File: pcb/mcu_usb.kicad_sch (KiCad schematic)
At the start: 33 parts, among them J12 USB_C_Receptacle, J13 UPDI, U10 CP2102N-A02-GQFN24, U11 LP2985-3.3, U9 AVR128DA32-I/PT, Y1 32.768kHz

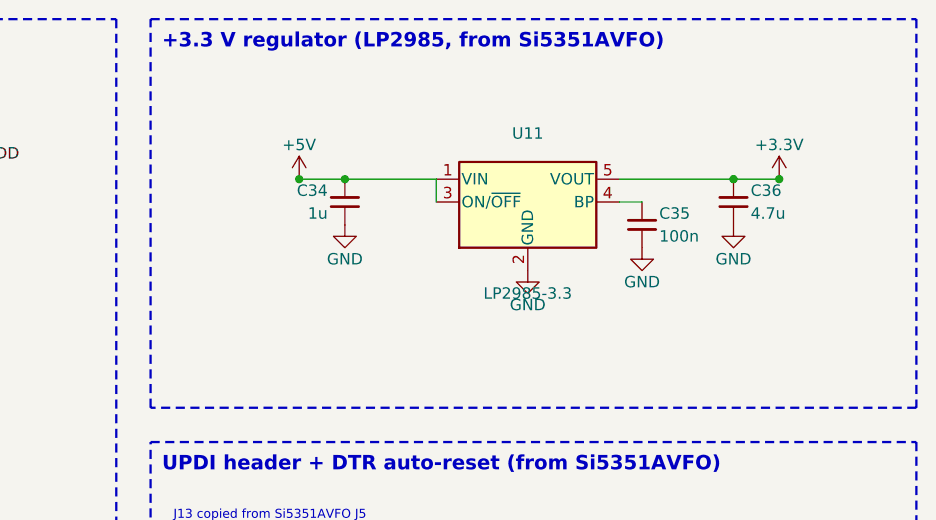
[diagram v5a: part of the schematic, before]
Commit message: GPS fixes: TPS22941 antenna current limit, TLV75533 500 mA LDO, CR1220 V_BCKP
- U13 TPS22941 (C2653762) limits antenna short to 40-80 mA with auto-restart
  (avg <= 27 mA, was 320 mA); OC -> SDA as ANT_SHORT_N (IM 3.3.1.2)
- U11 LP2985 -> TLV75533PDBVR (C404027), C35 removed (pin 4 NC)
- C47/D13/R41 removed; BT1 CR1220 in KH-BS1220-2-SMT (C5365932)
- VERIFY updated
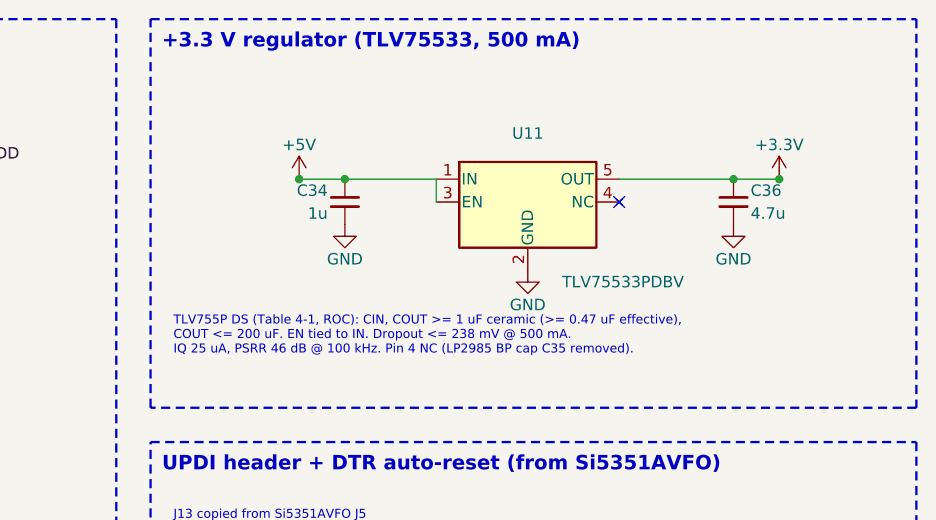
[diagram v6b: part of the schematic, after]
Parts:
- removed C35: 100n, Capacitor_SMD:C_0805_2012Metric, symbol Device:C_Small
- removed U11: LP2985-3.3, Package_TO_SOT_SMD:SOT-23-5, symbol Regulator_Linear:LP2985-3.3
- added U11: TLV75533PDBV, Package_TO_SOT_SMD:SOT-23-5, symbol OpenBeacon2:TLV75533PDBV
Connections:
- net +3.3V: now also U11.5 (OUT)
- net +5V: now also U11.1 (IN), U11.3 (EN)
- net GND: now also U11.2 (GND)
- no-connect marks 15 -> 16
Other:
- note added: "+3.3 V regulator (TLV75533, 500 mA)"
- note added: "TLV755P DS (Table 4-1, ROC): CIN, COUT >= 1 uF ceramic (>= 0.47 uF effective), COUT <= 200 uF. EN tied to IN. Dropout <= 238 mV @ 500 mA. IQ 25 uA, PSRR 46 dB @ 100 kHz. Pin 4 NC (LP2985 BP cap C35 removed)."
- note removed: "+3.3 V regulator (LP2985, from Si5351AVFO)"
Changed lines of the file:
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@@
 		)
 	)
-	(text "+3.3 V regulator (LP2985, from Si5351AVFO)"
+	(text "+3.3 V regulator (TLV75533, 500 mA)"
 		(exclude_from_sim no)
 		(at 200.66 22.86 0)
@@
 	)
 	(symbol
-		(lib_id "Regulator_Linear:LP2985-3.3")
+		(lib_id "OpenBeacon2:TLV75533PDBV")
 		(at 241.3 40.64 0)
 		(unit 1)
@@
 			)
 		)
-		(property "Value" "LP2985-3.3"
-			(at 241.3 50.8 0)
+		(property "Value" "TLV75533PDBV"
+			(at 245.11 49.53 0)
 			(effects
 				(font
 					(size 1.27 1.27)
 				)
+				(justify left)
 			)
 		)
@@
 			)
 		)
-		(property "Datasheet" ""
+		(property "Datasheet" "https://www.ti.com/lit/ds/symlink/tlv755p.pdf"
 			(at 241.3 40.64 0)
 			(effects
@@
 			)
 		)
-		(property "MPN" "LP2985AIM5-3.3/NOPB"
+		(property "MPN" "TLV75533PDBVR"
 			(at 241.3 40.64 0)
 			(effects
@@
 			)
 		)
-		(property "LCSC" "C16085"
+		(property "LCSC" "C404027"
 			(at 241.3 40.64 0)
 			(effects
@@
 		(pin "1"
 		)
-		(pin "2"
-		)
 		(pin "3"
 		)
+		(pin "2"
+		)
 		(pin "4"
 		)
@@
 		)
 	)
-	(wire
-		(pts
-			(xy 251.46 40.64)
-			(xy 254 40.64)
-		)
-		(stroke
-			(width 0)
-			(type default)
-		)
-	)
-	(symbol
-		(lib_id "Device:C_Small")
-		(at 254 43.18 0)
-		(unit 1)
-		(exclude_from_sim no)
-		(in_bom yes)
-		(on_board yes)
-		(dnp no)
-		(property "Reference" "C35"
-			(at 255.905 41.91 0)
-			(effects
-				(font
-					(size 1.27 1.27)
-				)
-				(justify left)
-			)
-		)
-		(property "Value" "100n"
-			(at 255.905 44.45 0)
-			(effects
-				(font
-					(size 1.27 1.27)
-				)
-				(justify left)
-			)
-		)
-		(property "Footprint" "Capacitor_SMD:C_0805_2012Metric"
-			(at 254 43.18 0)
-			(effects
-				(font
-					(size 1.27 1.27)
-				)
-				(hide yes)
-			)
-		)
-		(property "Datasheet" ""
-			(at 254 43.18 0)
-			(effects
-				(font
-					(size 1.27 1.27)
-				)
-				(hide yes)
-			)
-		)
-		(property "MPN" "CC0805KRX7R9BB104"
-			(at 254 43.18 0)
-			(effects
-				(font
-					(size 1.27 1.27)
-				)
-				(hide yes)
-			)
-		)
-		(property "Manufacturer" "YAGEO"
-			(at 254 43.18 0)
-			(effects
-				(font
-					(size 1.27 1.27)
-				)
-				(hide yes)
-			)
-		)
-		(property "LCSC" "C49678"
-			(at 254 43.18 0)
-			(effects
-				(font
-					(size 1.27 1.27)
-				)
-				(hide yes)
-			)
-		)
-		(pin "1"
-		)
-		(pin "2"
-		)
-		(instances
-			(project "OpenBeacon2"
-				(path "/046319a3-a6ce-4e59-a888-94e340127381/5d0c3a21-8e4b-4c7a-9a61-0b2f6e7a9c11"
-					(reference "C35")
-					(unit 1)
-				)
-			)
-		)
-	)
-	(symbol
-		(lib_id "power:GND")
-		(at 254 45.72 0)
-		(unit 1)
-		(exclude_from_sim no)
-		(in_bom no)
-		(on_board yes)
-		(dnp no)
-		(property "Reference" "#PWR923"
-			(at 254 45.72 0)
-			(effects
-				(font
-					(size 1.27 1.27)
-				)
-				(hide yes)
-			)
-		)
-		(property "Value" "GND"
-			(at 254 49.53 0)
-			(effects
-				(font
-					(size 1.27 1.27)
-				)
-			)
-		)
-		(property "Footprint" ""
-			(at 254 45.72 0)
-			(effects
-				(font
-					(size 1.27 1.27)
-				)
-				(hide yes)
-			)
-		)
-		(property "Datasheet" ""
-			(at 254 45.72 0)
-			(effects
-				(font
-					(size 1.27 1.27)
-				)
-				(hide yes)
-			)
-		)
-		(pin "1"
-		)
-		(instances
-			(project "OpenBeacon2"
-				(path "/046319a3-a6ce-4e59-a888-94e340127381/5d0c3a21-8e4b-4c7a-9a61-0b2f6e7a9c11"
-					(reference "#PWR923")
-					(unit 1)
-				)
-			)
-		)
+	(no_connect
+		(at 251.46 40.64)
 	)
 	(wire
@@
 		(on_board yes)
 		(dnp no)
-		(property "Reference" "#PWR924"
+		(property "Reference" "#PWR923"
 			(at 264.16 43.18 0)
 			(effects
@@
 			(project "OpenBeacon2"
 				(path "/046319a3-a6ce-4e59-a888-94e340127381/5d0c3a21-8e4b-4c7a-9a61-0b2f6e7a9c11"
-					(reference "#PWR924")
+					(reference "#PWR923")
 					(unit 1)
 				)
@@
 		(on_board yes)
 		(dnp no)
-		(property "Reference" "#PWR925"
+		(property "Reference" "#PWR924"
 			(at 269.24 38.1 0)
 			(effects
@@
 			(project "OpenBeacon2"
 				(path "/046319a3-a6ce-4e59-a888-94e340127381/5d0c3a21-8e4b-4c7a-9a61-0b2f6e7a9c11"
-					(reference "#PWR925")
+					(reference "#PWR924")
 					(unit 1)
 				)
@@
 		(color 0 0 0 0)
 	)
+	(text "TLV755P DS (Table 4-1, ROC): CIN, COUT >= 1 uF ceramic (>= 0.47 uF effective),\nCOUT <= 200 uF. EN tied to IN. Dropout <= 238 mV @ 500 mA.\nIQ 25 uA, PSRR 46 dB @ 100 kHz. Pin 4 NC (LP2985 BP cap C35 removed)."
+		(exclude_from_sim no)
+		(at 201.93 53.34 0)
+		(effects
+			(font
+				(size 1.0 1.0)
+			)
+			(justify left top)
+		)
+	)
 	(rectangle
 		(start 199.39 67.31)
@@
 		(on_board yes)
 		(dnp no)
-		(property "Reference" "#PWR926"
+		(property "Reference" "#PWR925"
 			(at 269.24 81.28 0)
 			(effects
@@
 			(project "OpenBeacon2"
 				(path "/046319a3-a6ce-4e59-a888-94e340127381/5d0c3a21-8e4b-4c7a-9a61-0b2f6e7a9c11"
-					(reference "#PWR926")
+					(reference "#PWR925")
 					(unit 1)
 				)
@@
 		(on_board yes)
 		(dnp no)
-		(property "Reference" "#PWR927"
+		(property "Reference" "#PWR926"
 			(at 269.24 88.9 0)
 			(effects
@@
 			(project "OpenBeacon2"
 				(path "/046319a3-a6ce-4e59-a888-94e340127381/5d0c3a21-8e4b-4c7a-9a61-0b2f6e7a9c11"
-					(reference "#PWR927")
+					(reference "#PWR926")
 					(unit 1)
 				)
@@
 		(on_board yes)
 		(dnp no)
-		(property "Reference" "#PWR928"
+		(property "Reference" "#PWR927"
 			(at 224.79 109.22 0)
 			(effects
@@
 			(project "OpenBeacon2"
 				(path "/046319a3-a6ce-4e59-a888-94e340127381/5d0c3a21-8e4b-4c7a-9a61-0b2f6e7a9c11"
-					(reference "#PWR928")
+					(reference "#PWR927")
 					(unit 1)
 				)
@@
 		(on_board yes)
 		(dnp no)
-		(property "Reference" "#PWR929"
+		(property "Reference" "#PWR928"
 			(at 91.44 116.84 0)
 			(effects
@@
 			(project "OpenBeacon2"
 				(path "/046319a3-a6ce-4e59-a888-94e340127381/5d0c3a21-8e4b-4c7a-9a61-0b2f6e7a9c11"
-					(reference "#PWR929")
+					(reference "#PWR928")
 					(unit 1)
 				)
@@
 		(on_board yes)
 		(dnp no)
-		(property "Reference" "#PWR930"
+		(property "Reference" "#PWR929"
 			(at 81.28 116.84 0)
 			(effects
@@
 			(project "OpenBeacon2"
 				(path "/046319a3-a6ce-4e59-a888-94e340127381/5d0c3a21-8e4b-4c7a-9a61-0b2f6e7a9c11"
-					(reference "#PWR930")
+					(reference "#PWR929")
 					(unit 1)
 				)
@@
 		(on_board yes)
 		(dnp no)
-		(property "Reference" "#PWR931"
+		(property "Reference" "#PWR930"
 			(at 99.06 111.76 0)
 			(effects
@@
 			(project "OpenBeacon2"
 				(path "/046319a3-a6ce-4e59-a888-94e340127381/5d0c3a21-8e4b-4c7a-9a61-0b2f6e7a9c11"
-					(reference "#PWR931")
+					(reference "#PWR930")
 					(unit 1)
 				)
@@
 		(on_board yes)
 		(dnp no)
-		(property "Reference" "#PWR932"
+		(property "Reference" "#PWR931"
 			(at 114.3 116.84 0)
 			(effects
@@
 			(project "OpenBeacon2"
 				(path "/046319a3-a6ce-4e59-a888-94e340127381/5d0c3a21-8e4b-4c7a-9a61-0b2f6e7a9c11"
-					(reference "#PWR932")
+					(reference "#PWR931")
 					(unit 1)
 				)
@@
 		(on_board yes)
 		(dnp no)
-		(property "Reference" "#PWR933"
+		(property "Reference" "#PWR932"
 			(at 106.68 111.76 0)
 			(effects
@@
 			(project "OpenBeacon2"
 				(path "/046319a3-a6ce-4e59-a888-94e340127381/5d0c3a21-8e4b-4c7a-9a61-0b2f6e7a9c11"
-					(reference "#PWR933")
+					(reference "#PWR932")
 					(unit 1)
 				)
@@
 		(on_board yes)
 		(dnp no)
-		(property "Reference" "#PWR934"
+		(property "Reference" "#PWR933"
 			(at 101.6 175.26 0)
 			(effects
@@
 			(project "OpenBeacon2"
 				(path "/046319a3-a6ce-4e59-a888-94e340127381/5d0c3a21-8e4b-4c7a-9a61-0b2f6e7a9c11"
-					(reference "#PWR934")
+					(reference "#PWR933")
 					(unit 1)
 				)
@@
 		(on_board yes)
 		(dnp no)
-		(property "Reference" "#PWR935"
+		(property "Reference" "#PWR934"
 			(at 58.42 144.78 0)
 			(effects
@@
 			(project "OpenBeacon2"
 				(path "/046319a3-a6ce-4e59-a888-94e340127381/5d0c3a21-8e4b-4c7a-9a61-0b2f6e7a9c11"
-					(reference "#PWR935")
+					(reference "#PWR934")
 					(unit 1)
 				)
@@
 		(on_board yes)
 		(dnp no)
-		(property "Reference" "#PWR936"
+		(property "Reference" "#PWR935"
 			(at 129.54 182.88 0)
 			(effects
@@
 			(project "OpenBeacon2"
 				(path "/046319a3-a6ce-4e59-a888-94e340127381/5d0c3a21-8e4b-4c7a-9a61-0b2f6e7a9c11"
-					(reference "#PWR936")
+					(reference "#PWR935")
 					(unit 1)
 				)
@@
 		(on_board yes)
 		(dnp no)
-		(property "Reference" "#PWR937"
+		(property "Reference" "#PWR936"
 			(at 139.7 180.34 0)
 			(effects
@@
 			(project "OpenBeacon2"
 				(path "/046319a3-a6ce-4e59-a888-94e340127381/5d0c3a21-8e4b-4c7a-9a61-0b2f6e7a9c11"
-					(reference "#PWR937")
+					(reference "#PWR936")
 					(unit 1)
 				)

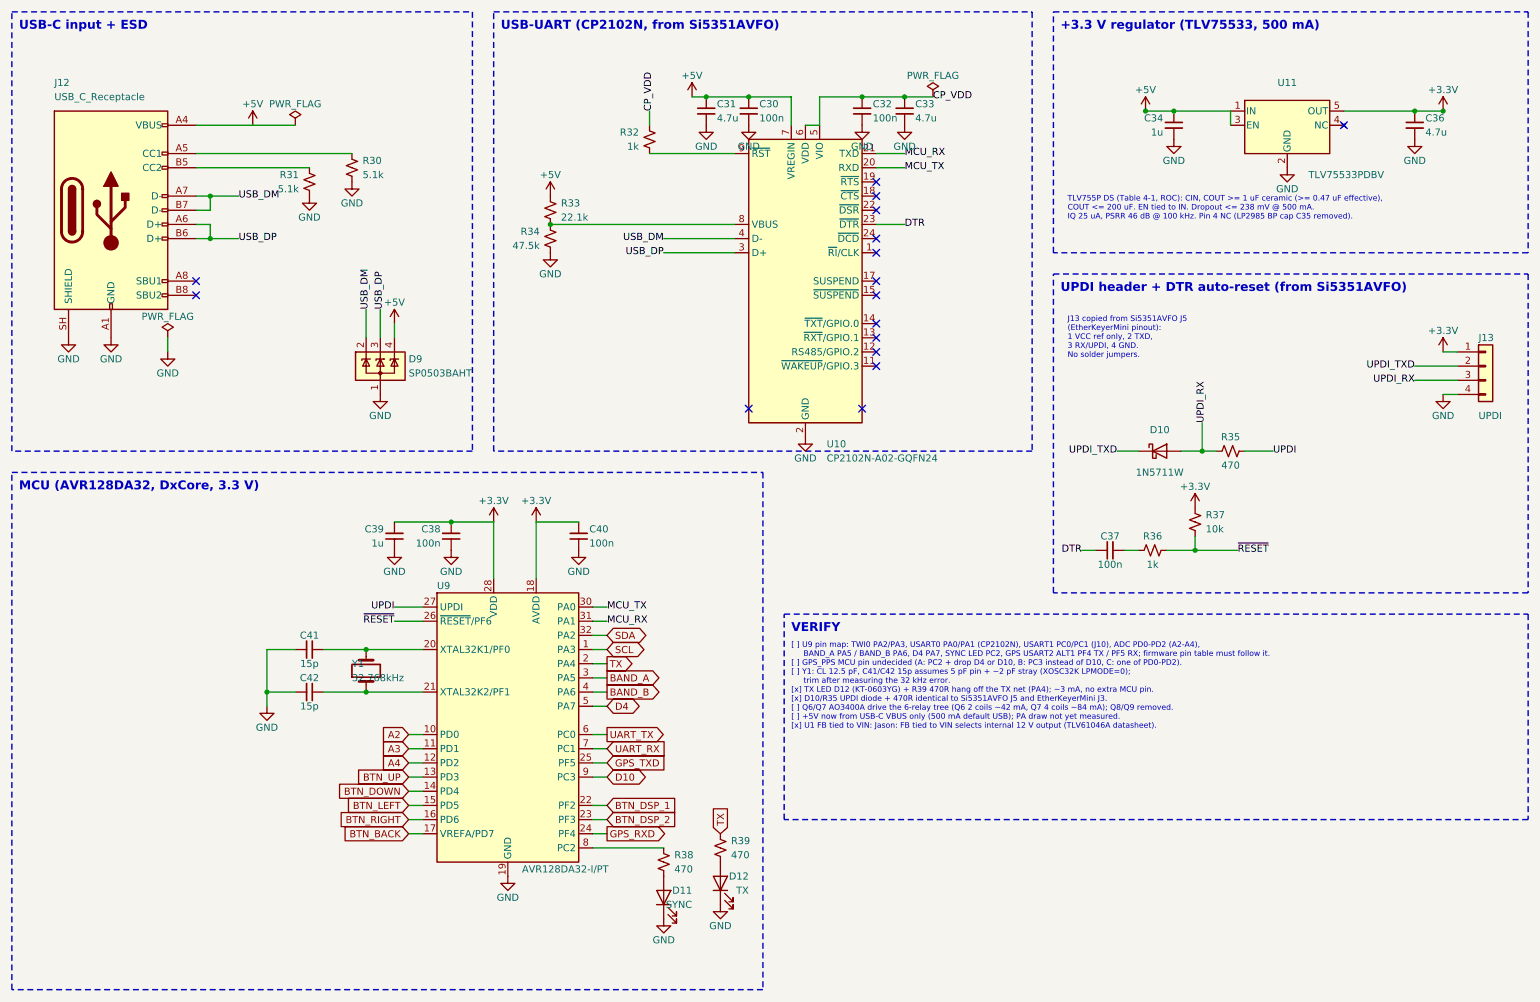
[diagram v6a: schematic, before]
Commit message: MCU: migrate to AVR128DA48-E/PT TQFP-48; GPS on USART3 PB0/PB1, GPS_PPS on async PF2 (EVSYS to TCB0 capture), per-pin decoupling
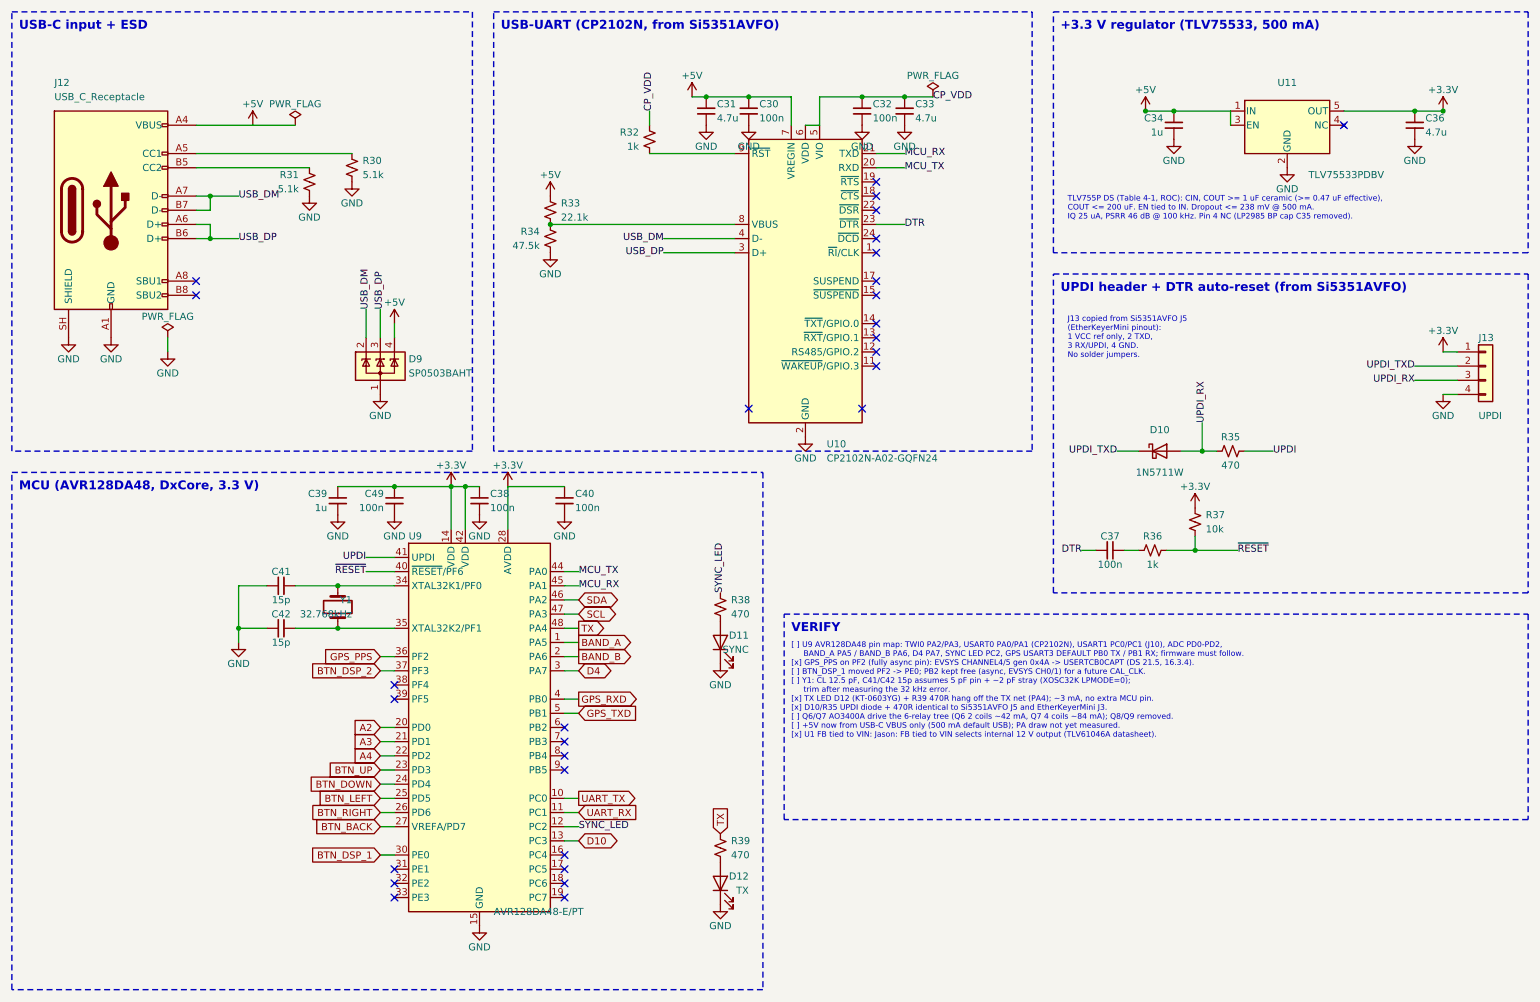
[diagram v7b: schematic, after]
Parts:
- removed U9: AVR128DA32-I/PT, Package_QFP:TQFP-32_7x7mm_P0.8mm, symbol OpenBeacon2:AVR128DA32x-xPT
- added C49: 100n, Capacitor_SMD:C_0603_1608Metric, symbol Device:C_Small
- added U9: AVR128DA48-E/PT, Package_QFP:TQFP-48_7x7mm_P0.5mm, symbol OpenBeacon2:AVR128DA48x-xPT
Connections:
- net +3.3V: now also C49.1, U9.14 (VDD), U9.28 (AVDD), U9.42 (VDD)
- net A2: now also U9.20 (PD0)
- net A3: now also U9.21 (PD1)
- net A4: now also U9.22 (PD2)
- net BAND_A: now also U9.1 (PA5)
- net BAND_B: now also U9.2 (PA6)
- net BTN_BACK: now also U9.27 (VREFA/PD7)
- net BTN_DOWN: now also U9.24 (PD4)
- net BTN_DSP_1: now also U9.30 (PE0)
- net BTN_DSP_2: now also U9.37 (PF3)
- net BTN_LEFT: now also U9.25 (PD5)
- net BTN_RIGHT: now also U9.26 (PD6)
- net BTN_UP: now also U9.23 (PD3)
- net D10: now also U9.13 (PC3)
- net D4: now also U9.3 (PA7)
- net GND: now also C49.2, U9.15 (GND), U9.29 (GND), U9.43 (GND)
- net GPS_RXD: now also U9.4 (PB0)
- net GPS_TXD: now also U9.5 (PB1)
- net MCU_RX: now also U9.45 (PA1)
- net MCU_TX: now also U9.44 (PA0)
- net SCL: now also U9.47 (PA3)
- net SDA: now also U9.46 (PA2)
- net TX: now also U9.48 (PA4)
- net UART_RX: now also U9.11 (PC1)
- net UART_TX: now also U9.10 (PC0)
- net UPDI: now also U9.41 (UPDI)
- net ~{RESET}: now also U9.40 (~{RESET}/PF6)
- net at C41.2, Y1.2: now also U9.34 (XTAL32K1/PF0)
- net SYNC_LED: now reaches R38.1
- net SYNC_LED: now also U9.12 (PC2)
- net at C42.2, Y1.1: now also U9.35 (XTAL32K2/PF1)
- new net GPS_PPS: U9.36 (PF2)
- no-connect marks 16 -> 29
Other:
- note added: "MCU (AVR128DA48, DxCore, 3.3 V)"
- note added: "[ ] U9 AVR128DA48 pin map: TWI0 PA2/PA3, USART0 PA0/PA1 (CP2102N), USART1 PC0/PC1 (J10), ADC PD0-PD2, BAND_A PA5 / BAND_B PA6, D4 PA7, SYNC LED PC2, GPS USART3 DEFAULT PB0 TX / PB1 RX; firmware must follow. [x] GPS_PPS on PF2 (fully async pin): EVSYS CHANNEL4/5 gen 0x4A -> USERTCB0CAPT (DS 21.5, 16.3.4). [ ] BTN_DSP_1 moved PF2 -> PE0; PB2 kept free (async, EVSYS CH0/1) for a future CAL_CLK. [ ] 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"
- note removed: "MCU (AVR128DA32, DxCore, 3.3 V)"
- note removed: "[ ] U9 pin map: TWI0 PA2/PA3, USART0 PA0/PA1 (CP2102N), USART1 PC0/PC1 (J10), ADC PD0-PD2 (A2-A4), BAND_A PA5 / BAND_B PA6, D4 PA7, SYNC LED PC2, GPS USART2 ALT1 PF4 TX / PF5 RX; firmware pin table must follow it. [ ] GPS_PPS MCU pin undecided (A: PC2 + drop D4 or D10, B: PC3 instead of D10, C: one of PD0-PD2). [ ] Y1: CL 12.5 pF, C41/C42 15p assumes 5 pF pin + ~2 pF stray (XOSC32K LPMODE=0); tri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"
